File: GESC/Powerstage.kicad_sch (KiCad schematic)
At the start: 30 parts, among them J1 gates, J2 gates, J3 gates, J4 SH1, J5 SH2, J6 SH3, Q1 TO-247, Q2 TO-247, Q3 TO-247, Q4 TO-247, Q5 TO-247, Q6 TO-247

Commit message: aaaaaaaaaaaaaaaaaaa
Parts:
- added C15, C16, C17, C18, C19, C20, C21, C22, C23, C24: 470nF, symbol Device:C
- added C25, C26, C27, C28: 330uF, symbol Device:C_Polarized
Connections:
- net GND: now also C15.2, C16.2, C17.2, C18.2, C19.2, C20.2, C21.2, C22.2, C23.2, C25.2, C26.2, C27.2, C28.2
- new net VBAT: C15.1, C16.1, C17.1, C18.1, C19.1, C20.1, C21.1, C22.1, C23.1, C25.1, C26.1, C27.1, C28.1
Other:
- title: (none) -> Power board
- moved on the sheet: J1, J2, J3, J4, J5, J6, Q1, Q2, Q3, Q4, Q5, Q6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

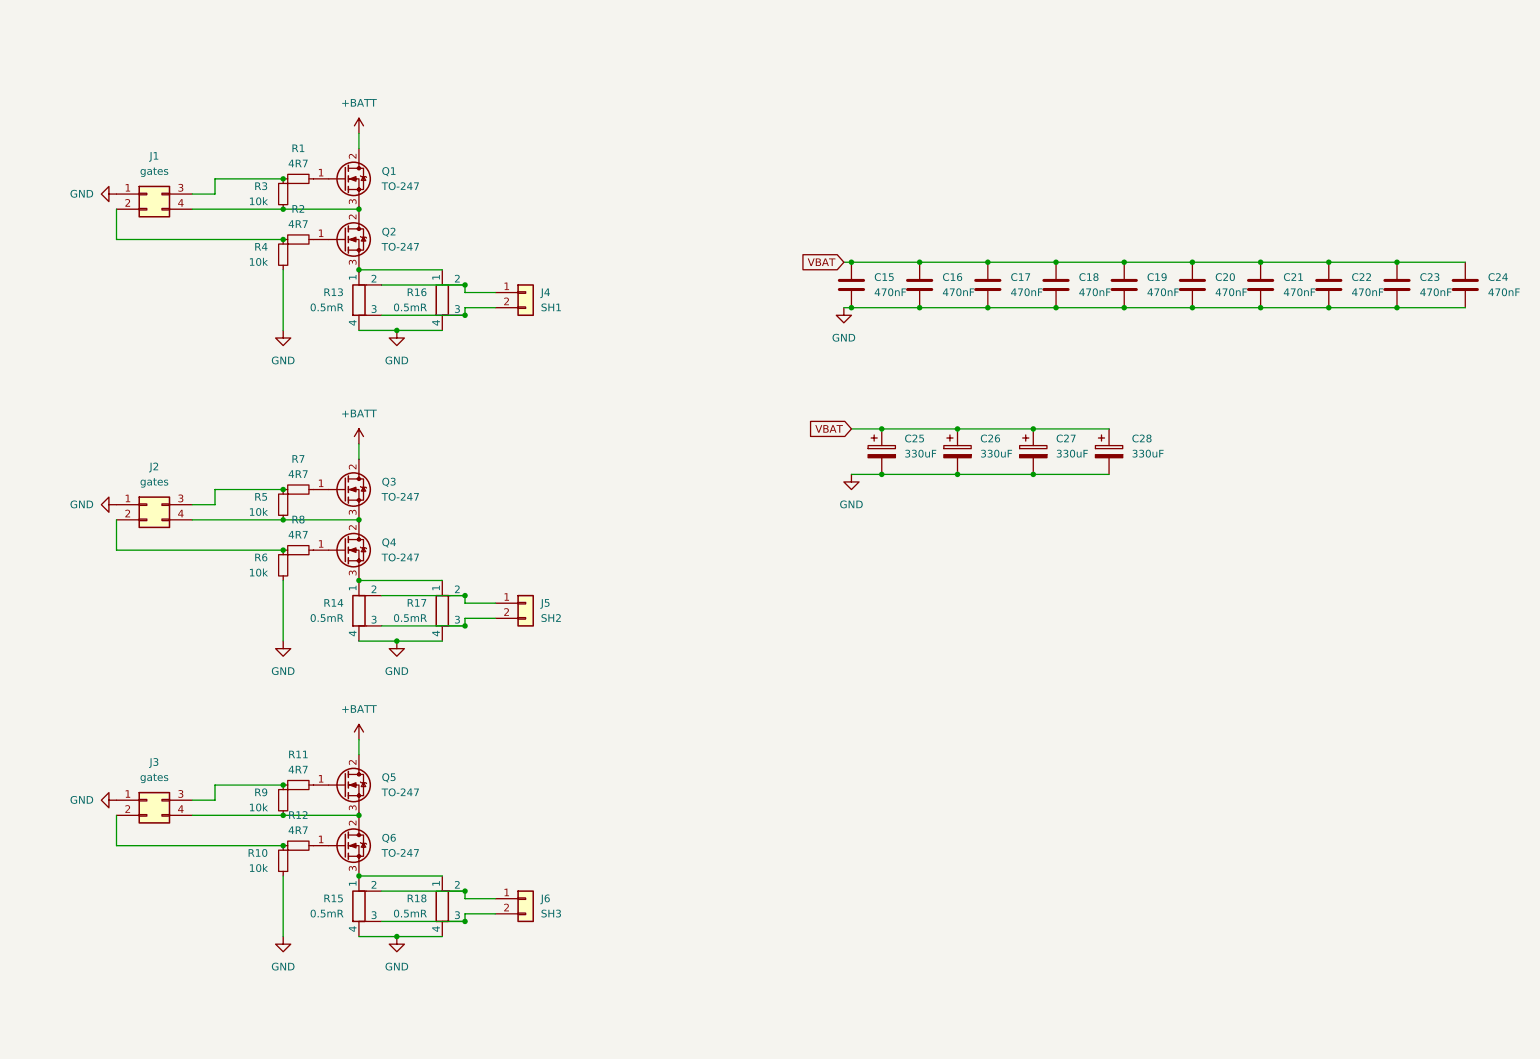
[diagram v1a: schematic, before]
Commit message: full to power board only
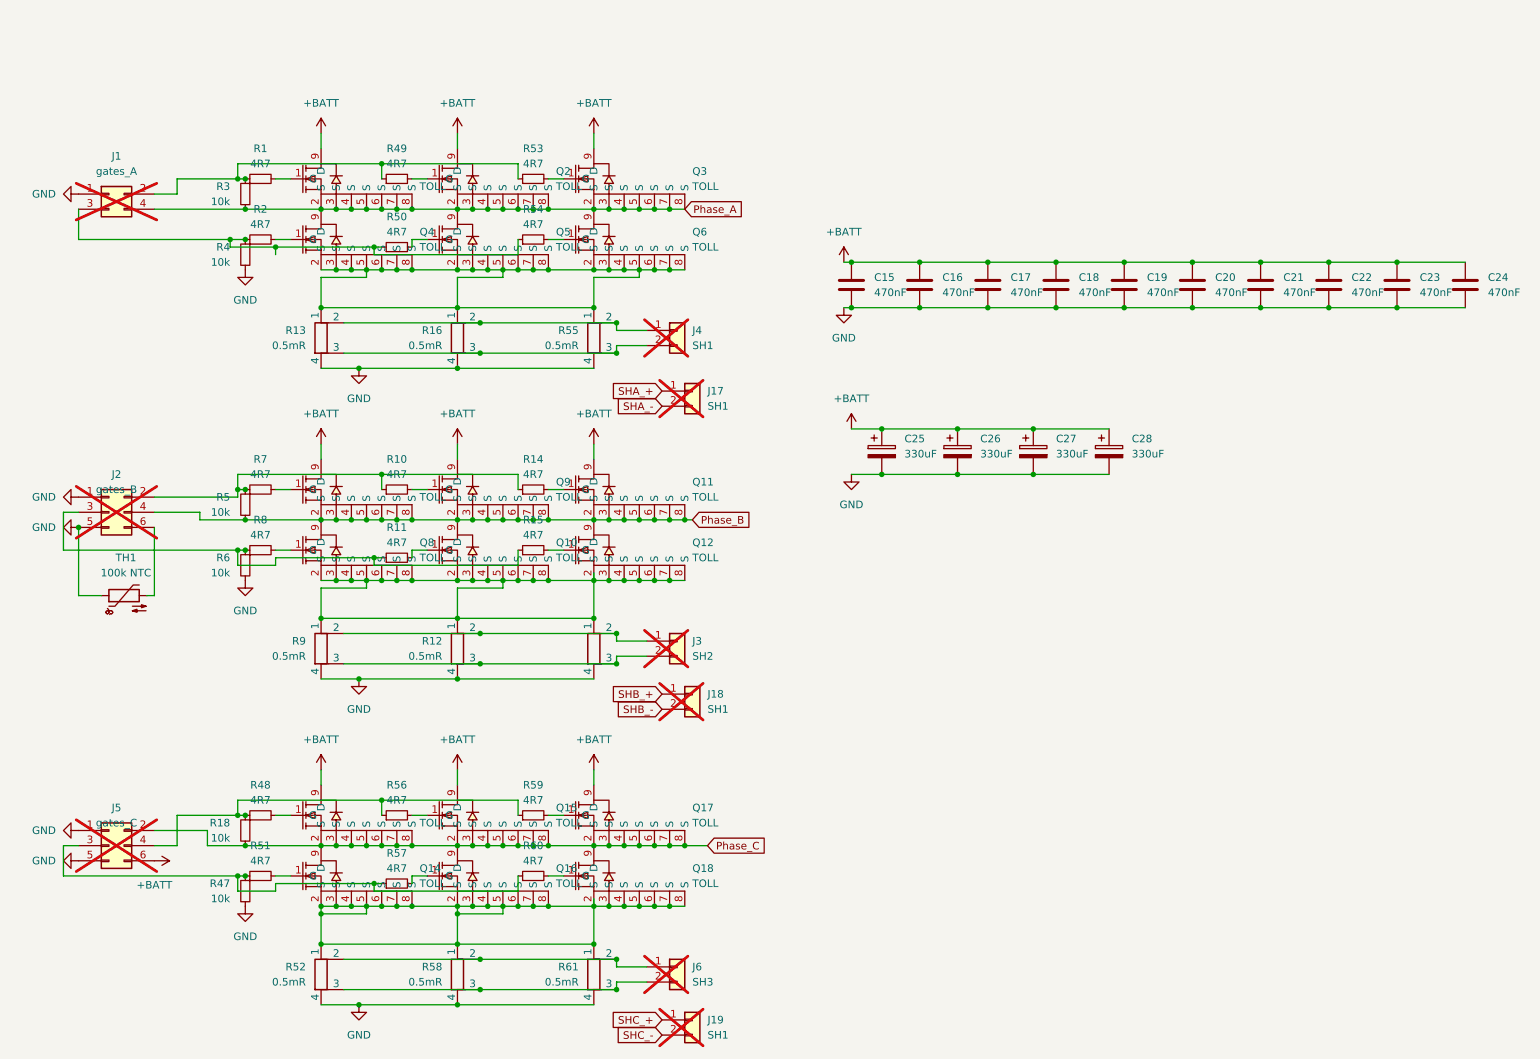
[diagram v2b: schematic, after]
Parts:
- removed J2, J3: gates, symbol Connector_Generic:Conn_02x02_Top_Bottom
- removed J5: SH2, symbol Connector_Generic:Conn_01x02
- removed Q3, Q4, Q5, Q6: TO-247, Package_TO_SOT_THT:TO-247-3_Vertical, symbol Transistor_FET:IRFP4668PbF
- removed R12: 4R7, symbol Device:R_Small
- removed R14, R15, R18: 0.5mR, symbol Device:R_Shunt
- removed R9: 10k, symbol Device:R_Small
- added J17, J18, J19: SH1, Connector_PinSocket_2.00mm:PinSocket_2x01_P2.00mm_Vertical_SMD, symbol Connector_Generic:Conn_01x02
- added J2: gates_B, Connector_PinHeader_2.00mm:PinHeader_2x03_P2.00mm_Vertical_SMD, symbol Connector_Generic:Conn_02x03_Odd_Even
- added J3: SH2, Connector_PinHeader_2.00mm:PinHeader_2x01_P2.00mm_Vertical_SMD, symbol Connector_Generic:Conn_01x02
- added J5: gates_C, Connector_PinHeader_2.00mm:PinHeader_2x03_P2.00mm_Vertical_SMD, symbol Connector_Generic:Conn_02x03_Odd_Even
- added Q10, Q11, Q12, Q13, Q14, Q15, Q16, Q17, Q18, Q2, Q3, Q5, Q6, Q7, Q8, Q9: TOLL, lcsc:TOLL-8_L10.4-W9.9-P1.20-LS11.7-BL, symbol easyeda:HYG015N10NS1TA
- added R12, R52, R55, R58, R61, R9: 0.5mR, lcsc:R3920, symbol Device:R_Shunt
- added R14, R15, R48, R49, R50, R51, R53, R54, R56, R57, R59, R60: 4R7, Resistor_SMD:R_0603_1608Metric, symbol Device:R_Small
- added R18, R47: 10k, Resistor_SMD:R_0603_1608Metric, symbol Device:R_Small
- added TH1: 100k NTC, Resistor_SMD:R_0402_1005Metric, symbol Device:Thermistor_NTC
- C15, C16, C17, C18, C19, C20, C21, C22, C23, C24: footprint (none) -> Capacitor_SMD:C_1210_3225Metric; LCSC Part (none) -> C192761
- C25, C26, C27, C28: footprint (none) -> lcsc:CAP-SMD_BD12.5-L13.5-W13.5-FD-1; LCSC Part (none) -> C487184
- J1: value gates -> gates_A; footprint (none) -> Connector_PinHeader_2.00mm:PinHeader_2x02_P2.00mm_Vertical_SMD; symbol Connector_Generic:Conn_02x02_Top_Bottom -> Connector_Generic:Conn_02x02_Odd_Even; now not fitted
- J4, J6: footprint (none) -> Connector_PinHeader_2.00mm:PinHeader_2x01_P2.00mm_Vertical_SMD; now not fitted
- Q1: value TO-247 -> TOLL; footprint Package_TO_SOT_THT:TO-247-3_Vertical -> lcsc:TOLL-8_L10.4-W9.9-P1.20-LS11.7-BL; symbol Transistor_FET:IRFP4668PbF -> easyeda:HYG015N10NS1TA; LCSC Part (none) -> C2979263
- Q4: renamed from Q2; value TO-247 -> TOLL; footprint Package_TO_SOT_THT:TO-247-3_Vertical -> lcsc:TOLL-8_L10.4-W9.9-P1.20-LS11.7-BL; symbol Transistor_FET:IRFP4668PbF -> easyeda:HYG015N10NS1TA; LCSC Part (none) -> C2979263
- R1, R11, R2, R7, R8: footprint (none) -> Resistor_SMD:R_0603_1608Metric; LCSC Part (none) -> C23164
- R10: value 10k -> 4R7; footprint (none) -> Resistor_SMD:R_0603_1608Metric; LCSC Part (none) -> C23164
- R13, R16, R17: footprint (none) -> lcsc:R3920; LCSC Part (none) -> C5224155
- R3, R4, R5, R6: footprint (none) -> Resistor_SMD:R_0603_1608Metric; LCSC Part (none) -> C2930027
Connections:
- net VBAT is gone; now on net +BATT: C15.1, C16.1, C17.1, C18.1, C19.1, C20.1, C21.1, C22.1, C23.1, C25.1, C26.1, C27.1, C28.1
- net +BATT: now also Q1.9 (D), J5.6 (Pin_6), Q11.9 (D), Q13.9 (D), Q15.9 (D), Q17.9 (D), Q2.9 (D), Q3.9 (D), Q7.9 (D), Q9.9 (D); no longer Q1.2 (D)
- net GND: now also J2.1 (Pin_1), J2.5 (Pin_5), J5.1 (Pin_1), J5.5 (Pin_5), R12.4, R47.2, R52.4, R55.4, R58.4, R61.4, R9.4, TH1.1; no longer R10.2
- net at R6.1, R8.1: now also R11.1, J2.3 (Pin_3), R15.1
- net at R2.1, R4.1: now also J1.3 (Pin_3), R50.1, R54.1; no longer J1.2 (Pin_2)
- net at R17.1: now also Q10.2 (S), Q10.3 (S), Q10.4 (S), Q10.5 (S), Q10.6 (S), Q10.7 (S), Q10.8 (S), Q12.2 (S), Q12.3 (S), Q12.4 (S), Q12.5 (S), Q12.6 (S), Q12.7 (S), Q12.8 (S), Q8.2 (S), Q8.3 (S), Q8.4 (S), Q8.5 (S), Q8.6 (S), Q8.7 (S), Q8.8 (S), R12.1, R9.1
- net at R17.2: now also J3.1 (Pin_1), R12.2, R9.2
- net at R17.3: now also J3.2 (Pin_2), R12.3, R9.3
- net at R1.1, R3.1: now also J1.2 (Pin_2), R49.1, R53.1; no longer J1.3 (Pin_3)
- net Phase_A: now reaches J1.4 (Pin_4), Q1.3 (S), R3.2
- net Phase_A: now also Q1.2 (S), Q1.4 (S), Q1.5 (S), Q1.6 (S), Q1.7 (S), Q1.8 (S), Q4.9 (D), Q2.2 (S), Q2.3 (S), Q2.4 (S), Q2.5 (S), Q2.6 (S), Q2.7 (S), Q2.8 (S), Q3.2 (S), Q3.3 (S), Q3.4 (S), Q3.5 (S), Q3.6 (S), Q3.7 (S), Q3.8 (S), Q5.9 (D), Q6.9 (D); no longer Q4.2 (D)
- net at R11.2: now also Q10.1 (G)
- net at Q4.3 (S), R13.1, R16.1: now also Q4.2 (S), Q4.4 (S), Q4.5 (S), Q4.6 (S), Q4.7 (S), Q4.8 (S), Q5.2 (S), Q5.3 (S), Q5.4 (S), Q5.5 (S), Q5.6 (S), Q5.7 (S), Q5.8 (S), Q6.2 (S), Q6.3 (S), Q6.4 (S), Q6.5 (S), Q6.6 (S), Q6.7 (S), Q6.8 (S), R55.1
- net at R8.2: now also Q8.1 (G)
- net at R5.1, R7.1: now also R10.1, J2.2 (Pin_2), R14.1
- net Phase_B: now reaches R5.2
- net Phase_B: now also J2.4 (Pin_4), Q10.9 (D), Q11.2 (S), Q11.3 (S), Q11.4 (S), Q11.5 (S), Q11.6 (S), Q11.7 (S), Q11.8 (S), Q12.9 (D), Q7.2 (S), Q7.3 (S), Q7.4 (S), Q7.5 (S), Q7.6 (S), Q7.7 (S), Q7.8 (S), Q8.9 (D), Q9.2 (S), Q9.3 (S), Q9.4 (S), Q9.5 (S), Q9.6 (S), Q9.7 (S), Q9.8 (S)
- net at J6.1 (Pin_1): now also R52.2, R58.2, R61.2
- net at J6.2 (Pin_2): now also R52.3, R58.3, R61.3
- net at R7.2: now also Q7.1 (G)
- net at J4.1 (Pin_1), R13.2, R16.2: now also R55.2
- net at J4.2 (Pin_2), R13.3, R16.3: now also R55.3
- new net: Q6.1 (G), R54.2
- new net: Q5.1 (G), R50.2
- new net: J2.6 (Pin_6), TH1.2
- new net: J5.3 (Pin_3), R47.1, R51.1, R57.1, R60.1
- new net: Q18.1 (G), R60.2
- new net: Q2.1 (G), R49.2
- new net: Q14.2 (S), Q14.3 (S), Q14.4 (S), Q14.5 (S), Q14.6 (S), Q14.7 (S), Q14.8 (S), Q16.2 (S), Q16.3 (S), Q16.4 (S), Q16.5 (S), Q16.6 (S), Q16.7 (S), Q16.8 (S), Q18.2 (S), Q18.3 (S), Q18.4 (S), Q18.5 (S), Q18.6 (S), Q18.7 (S), Q18.8 (S), R52.1, R58.1, R61.1
- new net: Q14.1 (G), R51.2
- new net: Q9.1 (G), R10.2
- new net: J5.4 (Pin_4), R18.1, R48.1, R56.1, R59.1
- new net: Q13.1 (G), R48.2
- new net: Q12.1 (G), R15.2
- new net: Q3.1 (G), R53.2
- new net: Q15.1 (G), R56.2
- new net: Q11.1 (G), R14.2
- new net: Q17.1 (G), R59.2
- new net: Q16.1 (G), R57.2
- new net Phase_C: J5.2 (Pin_2), Q13.2 (S), Q13.3 (S), Q13.4 (S), Q13.5 (S), Q13.6 (S), Q13.7 (S), Q13.8 (S), Q14.9 (D), Q15.2 (S), Q15.3 (S), Q15.4 (S), Q15.5 (S), Q15.6 (S), Q15.7 (S), Q15.8 (S), Q16.9 (D), Q17.2 (S), Q17.3 (S), Q17.4 (S), Q17.5 (S), Q17.6 (S), Q17.7 (S), Q17.8 (S), Q18.9 (D), R18.2
- new net SHA_+: J17.1 (Pin_1)
- new net SHA_-: J17.2 (Pin_2)
- new net SHB_+: J18.1 (Pin_1)
- new net SHB_-: J18.2 (Pin_2)
- new net SHC_+: J19.1 (Pin_1)
- new net SHC_-: J19.2 (Pin_2)
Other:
- moved on the sheet: R1, R13, R16, R2, R3, R4

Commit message: asdf
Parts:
- removed C25, C26, C27, C28: 330uF, lcsc:CAP-SMD_BD12.5-L13.5-W13.5-FD-1, symbol Device:C_Polarized
- removed J17, J18, J19: SH1, Connector_PinSocket_2.00mm:PinSocket_2x01_P2.00mm_Vertical_SMD, symbol Connector_Generic:Conn_01x02
- added C1, C10, C2, C3, C4, C5, C6, C7, C8, C9: 470nF, Capacitor_SMD:C_1210_3225Metric, symbol Device:C
- J3, J4, J6: footprint Connector_PinHeader_2.00mm:PinHeader_2x01_P2.00mm_Vertical_SMD -> Connector_PinHeader_2.00mm:PinHeader_1x02_P2.00mm_Vertical_SMD_Pin1Right; now fitted
- R12, R13, R16, R17, R52, R55, R58, R61, R9: value 0.5mR -> 0.2mR
- TH1: value 100k NTC -> 10k ntc; LCSC Part C77130 -> C13564
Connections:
- net +BATT: now also C24.1, C1.1, C10.1, C2.1, C3.1, C4.1, C5.1, C6.1, C7.1, C8.1, C9.1
- net GND: now also C24.2, J3.2 (Pin_2), J4.2 (Pin_2), J6.2 (Pin_2), R12.3, R13.3, R16.3, R17.3, R52.3, R55.3, R58.3, R61.3, R9.3, C1.2, C10.2, C2.2, C3.2, C4.2, C5.2, C6.2, C7.2, C8.2, C9.2
- net Phase_A: now also J5.4 (Pin_4); no longer J1.4 (Pin_4)
- net Phase_C: now also J1.2 (Pin_2); no longer J5.2 (Pin_2)
- net at Q4.2 (S), Q4.3 (S), Q4.4 (S)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: now also J4.1 (Pin_1), R13.2, R16.2, R55.2
- net at R2.1, R4.1, R50.1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: now also J5.3 (Pin_3); no longer J1.3 (Pin_3)
- net at Q10.2 (S), Q10.3 (S), Q10.4 (S)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: now also J3.1 (Pin_1), R12.2, R17.2, R9.2
- net at R47.1, R51.1, R57.1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: now also J1.3 (Pin_3); no longer J5.3 (Pin_3)
- net at R1.1, R3.1, R49.1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: now also J5.2 (Pin_2); no longer J1.2 (Pin_2)
- net at Q14.2 (S), Q14.3 (S), Q14.4 (S)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: now also J6.1 (Pin_1), R52.2, R58.2, R61.2
- net at R18.1, R48.1, R56.1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: now also J1.4 (Pin_4); no longer J5.4 (Pin_4)
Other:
- moved on the sheet: J1, J5
